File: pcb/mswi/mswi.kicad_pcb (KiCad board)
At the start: 2 copper layers, 140 x 72.3 mm, 0 parts

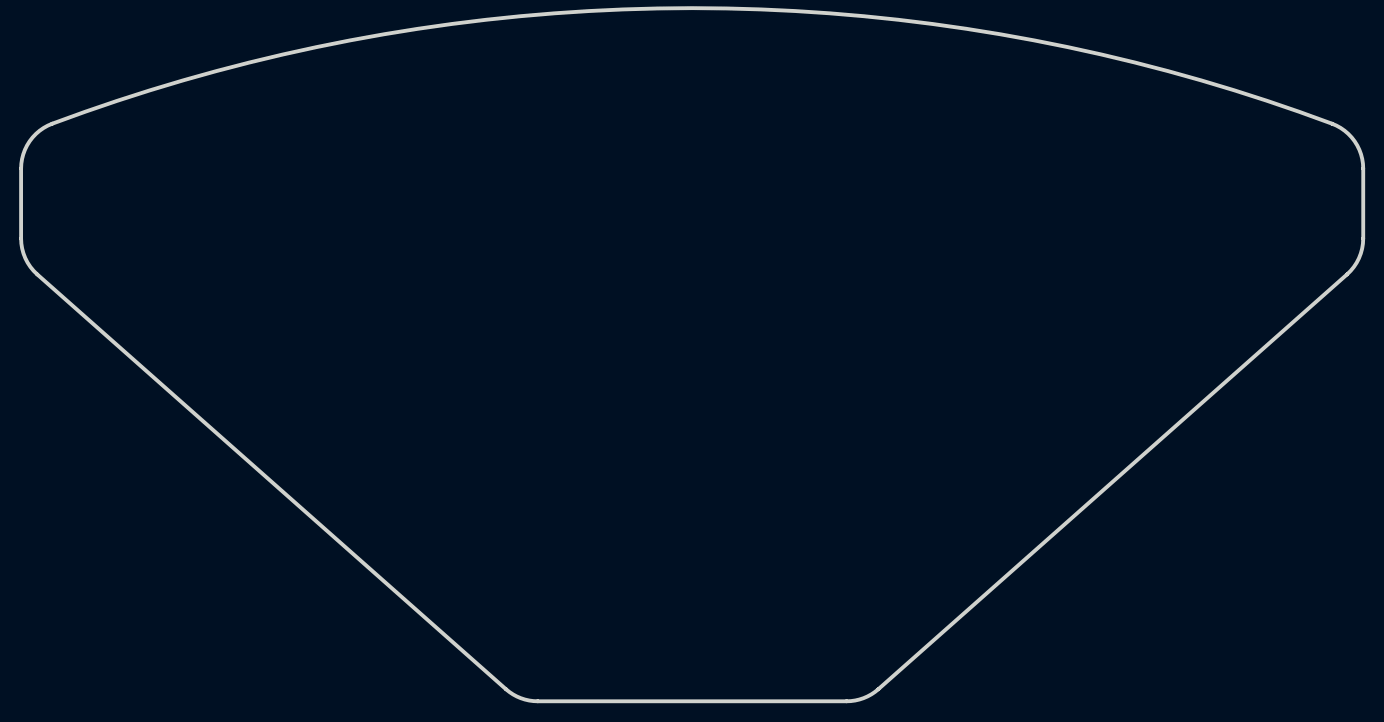
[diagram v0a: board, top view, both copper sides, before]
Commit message: Full schematic added. (To be revised).
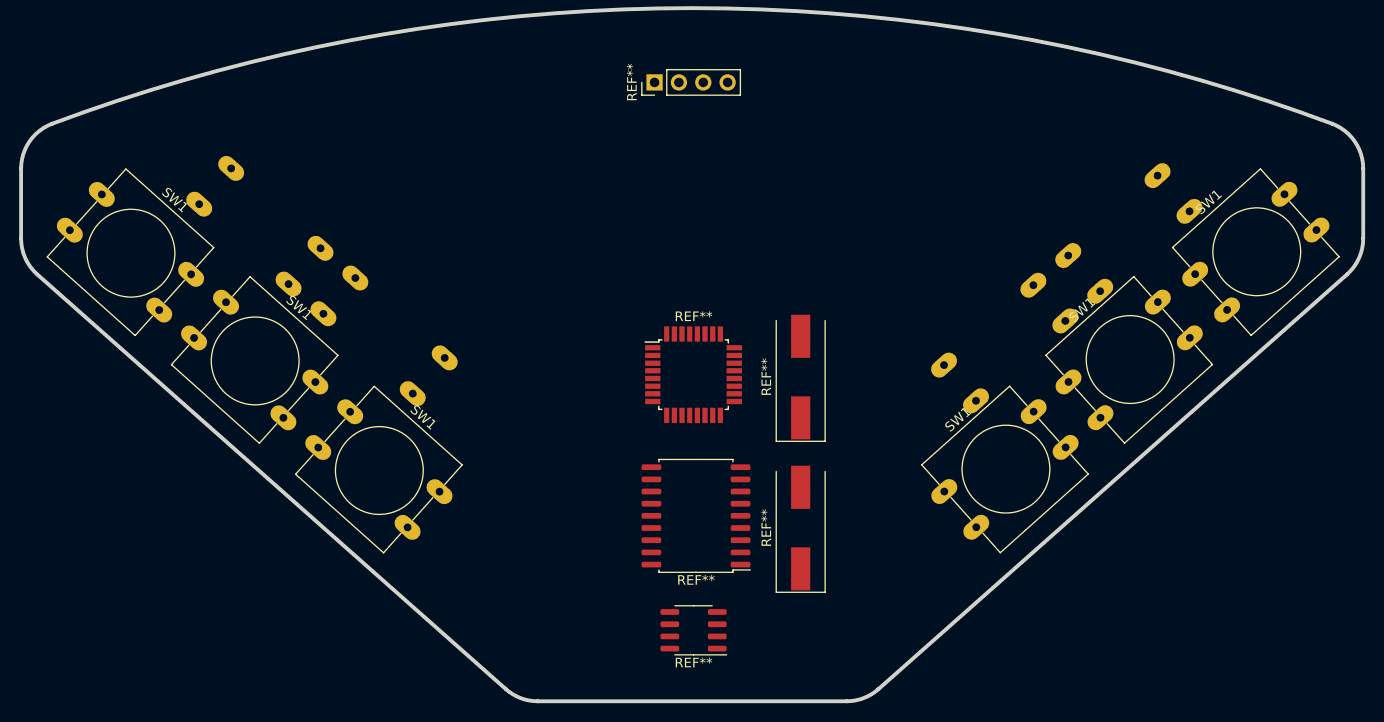
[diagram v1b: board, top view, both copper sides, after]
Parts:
- added REF**: Crystal_SMD_HC49-SD, Crystal:Crystal_SMD_HC49-SD, F.Cu at (157.2, 100.6)
- added REF**: Crystal_SMD_HC49-SD, Crystal:Crystal_SMD_HC49-SD, F.Cu at (157.2, 84.8)
- added REF**: PinHeader_1x04_P2.54mm_Vertical, Connector_PinHeader_2.54mm:PinHeader_1x04_P2.54mm_Vertical, F.Cu at (142.0, 54.1)
- added REF**: TQFP-32_7x7mm_P0.8mm, Package_QFP:TQFP-32_7x7mm_P0.8mm, F.Cu at (146.1, 84.6)
- added REF**: SOIC-8_3.9x4.9mm_P1.27mm, Package_SO:SOIC-8_3.9x4.9mm_P1.27mm, F.Cu at (146.1, 111.3)
- added REF**: SOIC-18W_7.5x11.6mm_P1.27mm, Package_SO:SOIC-18W_7.5x11.6mm_P1.27mm, F.Cu at (146.3, 99.3)
- added SW1: SW_Push_45deg, Button_Switch_THT:SW_PUSH-12mm, B.Cu at (188.5, 75.9)
- added SW1: SW_Push_45deg, Button_Switch_THT:SW_PUSH-12mm, F.Cu at (84.3, 65.8)
- added SW1: SW_Push_45deg, Button_Switch_THT:SW_PUSH-12mm, B.Cu at (175.5, 87.3)
- added SW1: SW_Push_45deg, Button_Switch_THT:SW_PUSH-12mm, F.Cu at (185.2, 85.3)
- added SW1: SW_Push_45deg, Button_Switch_THT:SW_PUSH-12mm, F.Cu at (198.4, 74.1)
- added SW1: SW_Push_45deg, Button_Switch_THT:SW_PUSH-12mm, F.Cu at (172.2, 96.8)
- added SW1: SW_Push_45deg, Button_Switch_THT:SW_PUSH-12mm, B.Cu at (94.5, 66.8)
- added SW1: SW_Push_45deg, Button_Switch_THT:SW_PUSH-12mm, B.Cu at (107.4, 78.2)
- added SW1: SW_Push_45deg, Button_Switch_THT:SW_PUSH-12mm, F.Cu at (110.2, 88.5)
- added SW1: SW_Push_45deg, Button_Switch_THT:SW_PUSH-12mm, F.Cu at (97.3, 77.0)

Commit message: renamed to avoid problems with KiCAD
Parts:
- removed REF** (x2): Crystal_SMD_HC49-SD, Crystal:Crystal_SMD_HC49-SD
- removed REF**: PinHeader_1x04_P2.54mm_Vertical, Connector_PinHeader_2.54mm:PinHeader_1x04_P2.54mm_Vertical
- removed REF**: TQFP-32_7x7mm_P0.8mm, Package_QFP:TQFP-32_7x7mm_P0.8mm
- removed REF**: SOIC-8_3.9x4.9mm_P1.27mm, Package_SO:SOIC-8_3.9x4.9mm_P1.27mm
- removed REF**: SOIC-18W_7.5x11.6mm_P1.27mm, Package_SO:SOIC-18W_7.5x11.6mm_P1.27mm
- removed SW1 (x10): SW_Push_45deg, Button_Switch_THT:SW_PUSH-12mm
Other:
- board outline removed

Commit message: components imported
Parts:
- added BZ301: Buzzer, Buzzer_Beeper:Buzzer_12x9.5RM7.6, F.Cu at (161.5, 101.3)
- added C201: 100nF, Capacitor_SMD:C_0805_2012Metric_Pad1.15x1.40mm_HandSolder, F.Cu at (91.5, 136.9)
- added C202: 100nF, Capacitor_SMD:C_0805_2012Metric_Pad1.15x1.40mm_HandSolder, F.Cu at (85.1, 141.4)
- added C203: 22pF, Capacitor_SMD:C_0805_2012Metric_Pad1.15x1.40mm_HandSolder, F.Cu at (93.5, 130.4)
- added C204: 22pF, Capacitor_SMD:C_0805_2012Metric_Pad1.15x1.40mm_HandSolder, F.Cu at (85.1, 144.4)
- added C205: 100nF, Capacitor_SMD:C_0805_2012Metric_Pad1.15x1.40mm_HandSolder, F.Cu at (98.2, 130.4)
- added C301: 100nF, Capacitor_SMD:C_0805_2012Metric_Pad1.15x1.40mm_HandSolder, F.Cu at (193.1, 91.4)
- added C302: 100nF, Capacitor_SMD:C_0805_2012Metric_Pad1.15x1.40mm_HandSolder, F.Cu at (194.4, 82.4)
- added C303: 100nF, Capacitor_SMD:C_0805_2012Metric_Pad1.15x1.40mm_HandSolder, F.Cu at (199.2, 85.3)
- added C304: 100nF, Capacitor_SMD:C_0805_2012Metric_Pad1.15x1.40mm_HandSolder, F.Cu at (179.2, 106.1)
- added C305: 22pF, Capacitor_SMD:C_0805_2012Metric_Pad1.15x1.40mm_HandSolder, F.Cu at (209.6, 79.1)
- added C306: 22pF, Capacitor_SMD:C_0805_2012Metric_Pad1.15x1.40mm_HandSolder, F.Cu at (194.4, 88.3)
- added C307: 100nF, Capacitor_SMD:C_0805_2012Metric_Pad1.15x1.40mm_HandSolder, F.Cu at (193.1, 94.3)
- added C308: 100nF, Capacitor_SMD:C_0805_2012Metric_Pad1.15x1.40mm_HandSolder, F.Cu at (184.1, 103.0)
- added C401: 1uF, Capacitor_SMD:C_0805_2012Metric_Pad1.15x1.40mm_HandSolder, F.Cu at (123.3, 107.5)
- added C402: 1uF, Capacitor_SMD:C_0805_2012Metric_Pad1.15x1.40mm_HandSolder, F.Cu at (145.1, 88.0)
- added C403: 1uF, Capacitor_SMD:C_0805_2012Metric_Pad1.15x1.40mm_HandSolder, F.Cu at (110.3, 122.7)
- added C404: 1uF, Capacitor_SMD:C_0805_2012Metric_Pad1.15x1.40mm_HandSolder, F.Cu at (137.6, 95.6)
- added C405: 1uF, Capacitor_SMD:C_0805_2012Metric_Pad1.15x1.40mm_HandSolder, F.Cu at (128.1, 104.6)
- added C406: 1uF, Capacitor_SMD:C_0805_2012Metric_Pad1.15x1.40mm_HandSolder, F.Cu at (132.8, 101.5)
- added C407: 1uF, Capacitor_SMD:C_0805_2012Metric_Pad1.15x1.40mm_HandSolder, F.Cu at (123.3, 110.5)
- added C408: 1uF, Capacitor_SMD:C_0805_2012Metric_Pad1.15x1.40mm_HandSolder, F.Cu at (145.1, 85.0)
- added C409: 1uF, Capacitor_SMD:C_0805_2012Metric_Pad1.15x1.40mm_HandSolder, F.Cu at (142.4, 90.9)
- added C410: 1uF, Capacitor_SMD:C_0805_2012Metric_Pad1.15x1.40mm_HandSolder, F.Cu at (149.9, 85.0)
- added C601: 1uF, Capacitor_SMD:C_0805_2012Metric_Pad1.15x1.40mm_HandSolder, F.Cu at (121.7, 136.7)
- added C602: 100nF, Capacitor_SMD:C_0805_2012Metric_Pad1.15x1.40mm_HandSolder, F.Cu at (121.7, 133.8)
- added C603: 100nF, Capacitor_SMD:C_0805_2012Metric_Pad1.15x1.40mm_HandSolder, F.Cu at (111.0, 138.5)
- added C604: 100nF, Capacitor_SMD:C_0805_2012Metric_Pad1.15x1.40mm_HandSolder, F.Cu at (125.7, 130.4)
- added C605: 100nF, Capacitor_SMD:C_0805_2012Metric_Pad1.15x1.40mm_HandSolder, F.Cu at (117.0, 138.1)
- added C606: 10uF, Capacitor_Tantalum_SMD:CP_EIA-6032-20_AVX-F_Pad2.25x2.35mm_HandSolder, F.Cu at (113.1, 131.3)
- added D201: pesd1can, Package_TO_SOT_SMD:SOT-23_Handsoldering, F.Cu at (85.9, 137.7)
- added D301: LL4148, Diode_SMD:D_MiniMELF_Handsoldering, F.Cu at (197.2, 79.3)
- added D302: LED_RED, LED_SMD:LED_0805_2012Metric_Pad1.15x1.40mm_HandSolder, F.Cu at (179.3, 103.1)
- added D303: LED_RED, LED_SMD:LED_0805_2012Metric_Pad1.15x1.40mm_HandSolder, F.Cu at (204.8, 79.2)
- added D304: LED_RED, LED_SMD:LED_0805_2012Metric_Pad1.15x1.40mm_HandSolder, F.Cu at (174.5, 103.1)
- added D305: LED_RED, LED_SMD:LED_0805_2012Metric_Pad1.15x1.40mm_HandSolder, F.Cu at (181.5, 85.8)
- added D401: LED_RED, LED_SMD:LED_0805_2012Metric_Pad1.15x1.40mm_HandSolder, F.Cu at (76.9, 119.8)
- added D402: LED_RED, LED_SMD:LED_0805_2012Metric_Pad1.15x1.40mm_HandSolder, F.Cu at (81.7, 119.8)
- added D403: LED_RED, LED_SMD:LED_0805_2012Metric_Pad1.15x1.40mm_HandSolder, F.Cu at (76.9, 122.9)
- added D404: LED_RED, LED_SMD:LED_0805_2012Metric_Pad1.15x1.40mm_HandSolder, F.Cu at (81.7, 122.9)
- added D405: LED_RED, LED_SMD:LED_0805_2012Metric_Pad1.15x1.40mm_HandSolder, F.Cu at (86.5, 119.8)
- added D406: LED_RED, LED_SMD:LED_0805_2012Metric_Pad1.15x1.40mm_HandSolder, F.Cu at (91.3, 119.8)
- added D407: LED_RED, LED_SMD:LED_0805_2012Metric_Pad1.15x1.40mm_HandSolder, F.Cu at (72.2, 119.8)
- added D408: LED_RED, LED_SMD:LED_0805_2012Metric_Pad1.15x1.40mm_HandSolder, F.Cu at (72.2, 122.9)
- added D409: LED_RED, LED_SMD:LED_0805_2012Metric_Pad1.15x1.40mm_HandSolder, F.Cu at (123.4, 92.7)
- added D410: LED_RED, LED_SMD:LED_0805_2012Metric_Pad1.15x1.40mm_HandSolder, F.Cu at (86.5, 122.9)
- added D601: MMSZ5240BT1, Diode_SMD:D_SOD-123, F.Cu at (120.4, 130.6)
- added F601: 500mA, Fuse:Fuse_1206_3216Metric_Pad1.42x1.75mm_HandSolder, F.Cu at (111.6, 135.3)
- added H101: MountingHole, MountingHole:MountingHole_3.2mm_M3, F.Cu at (170.5, 123.5)
- added H102: MountingHole, MountingHole:MountingHole_3.2mm_M3, F.Cu at (170.5, 115.6)
- added H103: MountingHole, MountingHole:MountingHole_3.2mm_M3, F.Cu at (162.5, 123.5)
- added H104: MountingHole, MountingHole:MountingHole_3.2mm_M3, F.Cu at (162.5, 115.6)
- added J301: AVR-ISP-6, Connector_IDC:IDC-Header_2x03_P2.54mm_Horizontal, F.Cu at (160.4, 83.6)
- added J302: USART, Connector_PinHeader_2.54mm:PinHeader_1x04_P2.54mm_Vertical, F.Cu at (189.7, 80.0)
- added J303: I2C, Connector_PinHeader_2.54mm:PinHeader_1x04_P2.54mm_Vertical, F.Cu at (176.8, 86.6)
- added J501: RJ45, KicadZeniteSolarLibrary18:RJ45_YH59_01, F.Cu at (111.0, 155.4)
- added L301: Bead, Inductor_SMD:L_0805_2012Metric_Pad1.15x1.40mm_HandSolder, F.Cu at (197.9, 91.2)
- added Q301: BC856, Package_TO_SOT_SMD:SOT-23, F.Cu at (174.3, 98.8)
- added Q401: BC856, Package_TO_SOT_SMD:SOT-23, F.Cu at (114.9, 123.5)
- added Q402: BC856, Package_TO_SOT_SMD:SOT-23, F.Cu at (137.4, 103.9)
- added Q403: BC856, Package_TO_SOT_SMD:SOT-23, F.Cu at (147.0, 93.3)
- added Q404: BC856, Package_TO_SOT_SMD:SOT-23, F.Cu at (119.7, 120.6)
- added Q405: BC856, Package_TO_SOT_SMD:SOT-23, F.Cu at (142.2, 97.6)
- added Q406: BC856, Package_TO_SOT_SMD:SOT-23, F.Cu at (123.2, 114.2)
- added Q407: BC856, Package_TO_SOT_SMD:SOT-23, F.Cu at (132.7, 105.3)
- added Q408: BC856, Package_TO_SOT_SMD:SOT-23, F.Cu at (137.4, 99.4)
- added Q409: BC856, Package_TO_SOT_SMD:SOT-23, F.Cu at (151.4, 93.3)
- added Q410: BC856, Package_TO_SOT_SMD:SOT-23, F.Cu at (127.9, 112.9)
- added Q411: BC856, Package_TO_SOT_SMD:SOT-23, F.Cu at (149.7, 88.8)
- added Q412: BC856, Package_TO_SOT_SMD:SOT-23, F.Cu at (141.9, 102.2)
- added Q413: BC856, Package_TO_SOT_SMD:SOT-23, F.Cu at (124.1, 118.8)
- added Q414: BC856, Package_TO_SOT_SMD:SOT-23, F.Cu at (146.6, 97.9)
- added Q415: BC856, Package_TO_SOT_SMD:SOT-23, F.Cu at (127.9, 108.3)
- added Q416: BC856, Package_TO_SOT_SMD:SOT-23, F.Cu at (132.4, 109.8)
- added Q417: BC856, Package_TO_SOT_SMD:SOT-23, F.Cu at (124.1, 123.3)
- added Q418: BC856, Package_TO_SOT_SMD:SOT-23, F.Cu at (141.9, 106.7)
- added Q419: BC856, Package_TO_SOT_SMD:SOT-23, F.Cu at (132.4, 114.4)
- added Q420: BC856, Package_TO_SOT_SMD:SOT-23, F.Cu at (137.1, 108.5)
- added Q601: si2308cds, Package_TO_SOT_SMD:SOT-23, F.Cu at (126.3, 134.2)
- added R201: 120, Resistor_SMD:R_0805_2012Metric_Pad1.15x1.40mm_HandSolder, F.Cu at (93.5, 133.4)
- added R202: 4k7, Resistor_SMD:R_0805_2012Metric_Pad1.15x1.40mm_HandSolder, F.Cu at (89.8, 141.4)
- added R203: 10k, Resistor_SMD:R_0805_2012Metric_Pad1.15x1.40mm_HandSolder, F.Cu at (96.2, 136.3)
- added R301: 100R, Resistor_SMD:R_0805_2012Metric_Pad1.15x1.40mm_HandSolder, F.Cu at (197.9, 97.1)
- added R302: 100R, Resistor_SMD:R_0805_2012Metric_Pad1.15x1.40mm_HandSolder, F.Cu at (208.7, 85.1)
- added R303: 100R, Resistor_SMD:R_0805_2012Metric_Pad1.15x1.40mm_HandSolder, F.Cu at (202.6, 91.2)
- added R304: 100R, Resistor_SMD:R_0805_2012Metric_Pad1.15x1.40mm_HandSolder, F.Cu at (197.9, 94.2)
- added R305: 1k, Resistor_SMD:R_0805_2012Metric_Pad1.15x1.40mm_HandSolder, F.Cu at (203.9, 88.1)
- added R306: 1k, Resistor_SMD:R_0805_2012Metric_Pad1.15x1.40mm_HandSolder, F.Cu at (193.1, 100.2)
- added R307: 1k, Resistor_SMD:R_0805_2012Metric_Pad1.15x1.40mm_HandSolder, F.Cu at (193.1, 97.3)
- added R308: 100R, Resistor_SMD:R_0805_2012Metric_Pad1.15x1.40mm_HandSolder, F.Cu at (184.1, 106.0)
- added R309: 100R, Resistor_SMD:R_0805_2012Metric_Pad1.15x1.40mm_HandSolder, F.Cu at (209.5, 82.2)
- added R310: 100R, Resistor_SMD:R_0805_2012Metric_Pad1.15x1.40mm_HandSolder, F.Cu at (197.9, 100.1)
- added R311: 10k, Resistor_SMD:R_0805_2012Metric_Pad1.15x1.40mm_HandSolder, F.Cu at (188.8, 103.2)
- added R312: 100R, Resistor_SMD:R_0805_2012Metric_Pad1.15x1.40mm_HandSolder, F.Cu at (199.2, 82.4)
- added R313: 100R, Resistor_SMD:R_0805_2012Metric_Pad1.15x1.40mm_HandSolder, F.Cu at (194.4, 85.3)
- added R314: 1k, Resistor_SMD:R_0805_2012Metric_Pad1.15x1.40mm_HandSolder, F.Cu at (174.5, 106.1)
- added R315: 1k, Resistor_SMD:R_0805_2012Metric_Pad1.15x1.40mm_HandSolder, F.Cu at (204.8, 82.2)
- added R316: 1k, Resistor_SMD:R_0805_2012Metric_Pad1.15x1.40mm_HandSolder, F.Cu at (193.6, 103.2)
- added R317: 1k, Resistor_SMD:R_0805_2012Metric_Pad1.15x1.40mm_HandSolder, F.Cu at (203.9, 85.1)
- added R318: 100R, Resistor_SMD:R_0805_2012Metric_Pad1.15x1.40mm_HandSolder, F.Cu at (199.2, 88.3)
- added R319: 100R, Resistor_SMD:R_0805_2012Metric_Pad1.15x1.40mm_HandSolder, F.Cu at (188.8, 106.1)
- added R401: 1k, Resistor_SMD:R_0805_2012Metric_Pad1.15x1.40mm_HandSolder, F.Cu at (149.9, 82.1)
- added R402: 1k, Resistor_SMD:R_0805_2012Metric_Pad1.15x1.40mm_HandSolder, F.Cu at (132.8, 98.6)
- added R403: 1k, Resistor_SMD:R_0805_2012Metric_Pad1.15x1.40mm_HandSolder, F.Cu at (115.1, 119.8)
- added R404: 1k, Resistor_SMD:R_0805_2012Metric_Pad1.15x1.40mm_HandSolder, F.Cu at (142.4, 93.9)
- added R405: 1k, Resistor_SMD:R_0805_2012Metric_Pad1.15x1.40mm_HandSolder, F.Cu at (140.4, 79.1)
- added R406: 1k, Resistor_SMD:R_0805_2012Metric_Pad1.15x1.40mm_HandSolder, F.Cu at (96.1, 122.7)
- added R407: 1k, Resistor_SMD:R_0805_2012Metric_Pad1.15x1.40mm_HandSolder, F.Cu at (100.8, 119.8)
- added R408: 1k, Resistor_SMD:R_0805_2012Metric_Pad1.15x1.40mm_HandSolder, F.Cu at (100.8, 122.7)
- added R409: 1k, Resistor_SMD:R_0805_2012Metric_Pad1.15x1.40mm_HandSolder, F.Cu at (128.1, 95.7)
- added R410: 1k, Resistor_SMD:R_0805_2012Metric_Pad1.15x1.40mm_HandSolder, F.Cu at (145.1, 82.1)
- added R411: 100, Resistor_SMD:R_0805_2012Metric_Pad1.15x1.40mm_HandSolder, F.Cu at (132.9, 92.7)
- added R412: 100, Resistor_SMD:R_0805_2012Metric_Pad1.15x1.40mm_HandSolder, F.Cu at (123.3, 101.6)
- added R413: 100, Resistor_SMD:R_0805_2012Metric_Pad1.15x1.40mm_HandSolder, F.Cu at (128.1, 92.7)
- added R414: 100, Resistor_SMD:R_0805_2012Metric_Pad1.15x1.40mm_HandSolder, F.Cu at (140.4, 82.1)
- added R415: 100, Resistor_SMD:R_0805_2012Metric_Pad1.15x1.40mm_HandSolder, F.Cu at (145.1, 79.1)
- added R416: 1k, Resistor_SMD:R_0805_2012Metric_Pad1.15x1.40mm_HandSolder, F.Cu at (91.3, 122.8)
- added R417: 1k, Resistor_SMD:R_0805_2012Metric_Pad1.15x1.40mm_HandSolder, F.Cu at (140.4, 85.0)
- added R418: 1k, Resistor_SMD:R_0805_2012Metric_Pad1.15x1.40mm_HandSolder, F.Cu at (96.1, 119.8)
- added R419: 1k, Resistor_SMD:R_0805_2012Metric_Pad1.15x1.40mm_HandSolder, F.Cu at (123.3, 95.7)
- added R420: 1k, Resistor_SMD:R_0805_2012Metric_Pad1.15x1.40mm_HandSolder, F.Cu at (123.3, 98.7)
- added R421: 1k, Resistor_SMD:R_0805_2012Metric_Pad1.15x1.40mm_HandSolder, F.Cu at (110.3, 119.8)
- added R422: 1k, Resistor_SMD:R_0805_2012Metric_Pad1.15x1.40mm_HandSolder, F.Cu at (137.6, 92.7)
- added R423: 1k, Resistor_SMD:R_0805_2012Metric_Pad1.15x1.40mm_HandSolder, F.Cu at (128.1, 101.6)
- added R424: 1k, Resistor_SMD:R_0805_2012Metric_Pad1.15x1.40mm_HandSolder, F.Cu at (105.6, 122.7)
- added R425: 1k, Resistor_SMD:R_0805_2012Metric_Pad1.15x1.40mm_HandSolder, F.Cu at (105.6, 119.8)
- added R426: 100, Resistor_SMD:R_0805_2012Metric_Pad1.15x1.40mm_HandSolder, F.Cu at (128.1, 98.7)
- added R427: 100, Resistor_SMD:R_0805_2012Metric_Pad1.15x1.40mm_HandSolder, F.Cu at (123.3, 104.6)
- added R428: 100, Resistor_SMD:R_0805_2012Metric_Pad1.15x1.40mm_HandSolder, F.Cu at (132.8, 95.6)
- added R429: 100, Resistor_SMD:R_0805_2012Metric_Pad1.15x1.40mm_HandSolder, F.Cu at (140.4, 88.0)
- added R430: 100, Resistor_SMD:R_0805_2012Metric_Pad1.15x1.40mm_HandSolder, F.Cu at (149.9, 79.1)
- added R601: 1M, Resistor_SMD:R_0805_2012Metric_Pad1.15x1.40mm_HandSolder, F.Cu at (117.0, 135.2)
- added SW401: SW_Push, Button_Switch_THT:SW_PUSH-12mm, F.Cu at (89.1, 95.5)
- added SW402: SW_Push, Button_Switch_THT:SW_PUSH-12mm, F.Cu at (106.2, 81.9)
- added SW403: SW_Push, Button_Switch_THT:SW_PUSH-12mm, F.Cu at (106.2, 109.0)
- added SW404: SW_Push, Button_Switch_THT:SW_PUSH-12mm, F.Cu at (89.1, 109.0)
- added SW405: SW_Push, Button_Switch_THT:SW_PUSH-12mm, F.Cu at (106.2, 95.5)
- added SW406: SW_Push, Button_Switch_THT:SW_PUSH-12mm, F.Cu at (123.2, 81.9)
- added SW407: SW_Push, Button_Switch_THT:SW_PUSH-12mm, F.Cu at (72.0, 81.9)
- added SW408: SW_Push, Button_Switch_THT:SW_PUSH-12mm, F.Cu at (89.1, 81.9)
- added SW409: SW_Push, Button_Switch_THT:SW_PUSH-12mm, F.Cu at (72.0, 109.0)
- added SW410: SW_Push, Button_Switch_THT:SW_PUSH-12mm, F.Cu at (72.0, 95.5)
- added TP201: SI, TestPoint:TestPoint_Pad_2.0x2.0mm, F.Cu at (102.3, 143.1)
- added TP202: SO, TestPoint:TestPoint_Pad_2.0x2.0mm, F.Cu at (98.3, 143.9)
- added TP203: TXCAN, TestPoint:TestPoint_Pad_2.0x2.0mm, F.Cu at (102.3, 139.1)
- added TP204: RXCAN, TestPoint:TestPoint_Pad_2.0x2.0mm, F.Cu at (98.3, 139.8)
- added TP205: SC, TestPoint:TestPoint_Pad_2.0x2.0mm, F.Cu at (93.5, 144.9)
- added TP206: SCK, TestPoint:TestPoint_Pad_2.0x2.0mm, F.Cu at (100.6, 135.0)
- added TP207: CAN_H, TestPoint:TestPoint_Pad_2.0x2.0mm, F.Cu at (94.2, 140.4)
- added TP208: CAN_L, TestPoint:TestPoint_Pad_2.0x2.0mm, F.Cu at (102.6, 131.0)
- added TP209: INT, TestPoint:TestPoint_Pad_2.0x2.0mm, F.Cu at (89.5, 144.9)
- added TP301: TX, TestPoint:TestPoint_Pad_2.0x2.0mm, F.Cu at (202.3, 94.7)
- added TP302: RX, TestPoint:TestPoint_Pad_2.0x2.0mm, F.Cu at (210.4, 92.7)
- added TP303: RST, TestPoint:TestPoint_Pad_2.0x2.0mm, F.Cu at (206.3, 98.8)
- added TP304: SDA, TestPoint:TestPoint_Pad_2.0x2.0mm, F.Cu at (198.0, 103.6)
- added TP305: SCL, TestPoint:TestPoint_Pad_2.0x2.0mm, F.Cu at (202.3, 98.8)
- added TP306: BUZZ_in, TestPoint:TestPoint_Pad_2.0x2.0mm, F.Cu at (206.3, 94.7)
- added TP307: BUZZ_out, TestPoint:TestPoint_Pad_2.0x2.0mm, F.Cu at (208.3, 88.6)
- added U201: MCP2551-I/SN, Package_SO:SOIC-8_3.9x4.9mm_P1.27mm, F.Cu at (86.9, 132.2)
- added U202: MCP2515-xSO, Package_SO:SOIC-18W_7.5x11.6mm_P1.27mm, F.Cu at (76.2, 135.5)
- added U301: ATmega328PB-AU, Package_QFP:TQFP-32_7x7mm_P0.8mm, F.Cu at (184.9, 95.7)
- added U601: LM7805, KicadZeniteSolarLibrary18:TO-220-3_Horizontal_TabDown_SMD, F.Cu at (137.9, 130.8)
- added Y201: 16MHz, Crystal:Crystal_HC49-U_Vertical, F.Cu at (73.8, 145.4)
- added Y301: 16MHz, Crystal:Crystal_HC49-U_Vertical, F.Cu at (178.5, 81.0)
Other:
- net class Default: clearance 0.2 -> 0.508; trace_width 0.25 -> 0.508; via_dia 0.8 -> 1.5; via_drill 0.4 -> 0.8
- rule pad_to_mask_clearance: 0.051 -> 0
- rule trace_clearance: 0.2 -> 0.508

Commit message: TODO list added
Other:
- board text added: "TODO: - OLED: Footprint & 3D - SW: 3D - PCB Geometry"
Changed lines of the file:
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@@
   (general
     (thickness 1.6)
-    (drawings 0)
+    (drawings 1)
     (tracks 0)
     (zones 0)
@@
     )
   )
+  (gr_text "TODO:\n- OLED: Footprint & 3D\n- SW: 3D\n- PCB Geometry\n" (at 249.174 145.288) (layer Eco2.User)
+    (effects (font (size 1.5 1.5) (thickness 0.3)) (justify left))
+  )
 )

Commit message: TODO list updated
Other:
- board text added: "TODO: - ISP: Change to Horizontal Version - OLED: Footprint & 3D - SW: 3D - RJ45: 3D - Fuse: 3D - PCB Geometry - Add zenitesolar and designer identification - Add opensource hardware symbol"
- board text removed: "TODO: - OLED: Footprint & 3D - SW: 3D - PCB Geometry"
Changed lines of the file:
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@@
     )
   )
-  (gr_text "TODO:\n- OLED: Footprint & 3D\n- SW: 3D\n- PCB Geometry\n" (at 249.174 145.288) (layer Eco2.User)
+  (gr_text "TODO:\n- ISP: Change to Horizontal Version\n- OLED: Footprint & 3D\n- SW: 3D\n- RJ45: 3D\n- Fuse: 3D\n- PCB Geometry\n- Add zenitesolar and designer identification\n- Add opensource hardware symbol" (at 227.838 151.384) (layer Eco2.User)
     (effects (font (size 1.5 1.5) (thickness 0.3)) (justify left))
   )

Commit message: PCB geometry added
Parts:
- moved BZ301 188.0 mm to (89.5, -72.3)
- moved C201 188.0 mm to (19.4, -36.8)
- moved C202 188.0 mm to (13.0, -32.2)
- moved C203 188.0 mm to (21.4, -43.2)
- moved C204 188.0 mm to (13.0, -29.3)
- moved C205 188.0 mm to (26.2, -43.2)
- moved C301 188.0 mm to (121.0, -82.2)
- moved C302 188.0 mm to (122.3, -91.2)
- moved C303 188.0 mm to (127.1, -88.3)
- moved C304 188.0 mm to (107.2, -67.5)
- moved C305 188.0 mm to (137.5, -94.5)
- moved C306 188.0 mm to (122.3, -85.3)
- moved C307 188.0 mm to (121.0, -79.3)
- moved C308 188.0 mm to (112.0, -70.6)
- moved C401 188.0 mm to (51.3, -66.1)
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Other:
- board outline added: 140 x 72.3 mm
- board text added: "140,00"
- board text added: "72,30"
- board text added: "TODO: [_] ISP: Change to Horizontal Version [_] OLED: Footprint & 3D [_] SW: 3D [_] RJ45: 3D [_] Fuse: 3D [x] PCB Geometry [_] Add zenitesolar and designer identification [_] Add opensource hardware symbol"
- board text removed: "TODO: - ISP: Change to Horizontal Version - OLED: Footprint & 3D - SW: 3D - RJ45: 3D - Fuse: 3D - PCB Geometry - Add zenitesolar and designer identification - Add opensource hardware symbol"
